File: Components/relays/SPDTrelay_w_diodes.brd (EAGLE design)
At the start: 27.9 x 41.6 mm, 3 parts, among them K1 PY14-02

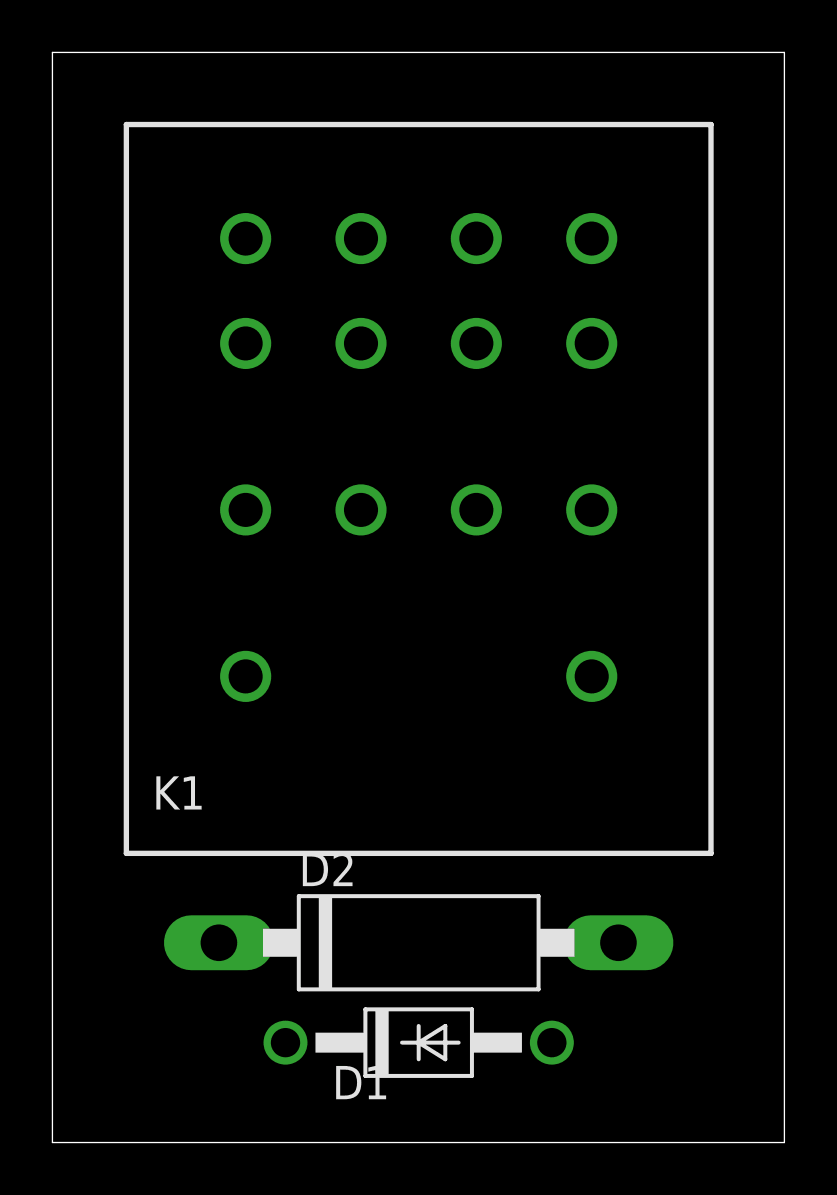
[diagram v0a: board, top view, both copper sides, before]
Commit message: Creating re-usable suppressed relay components w/ vertical diodes
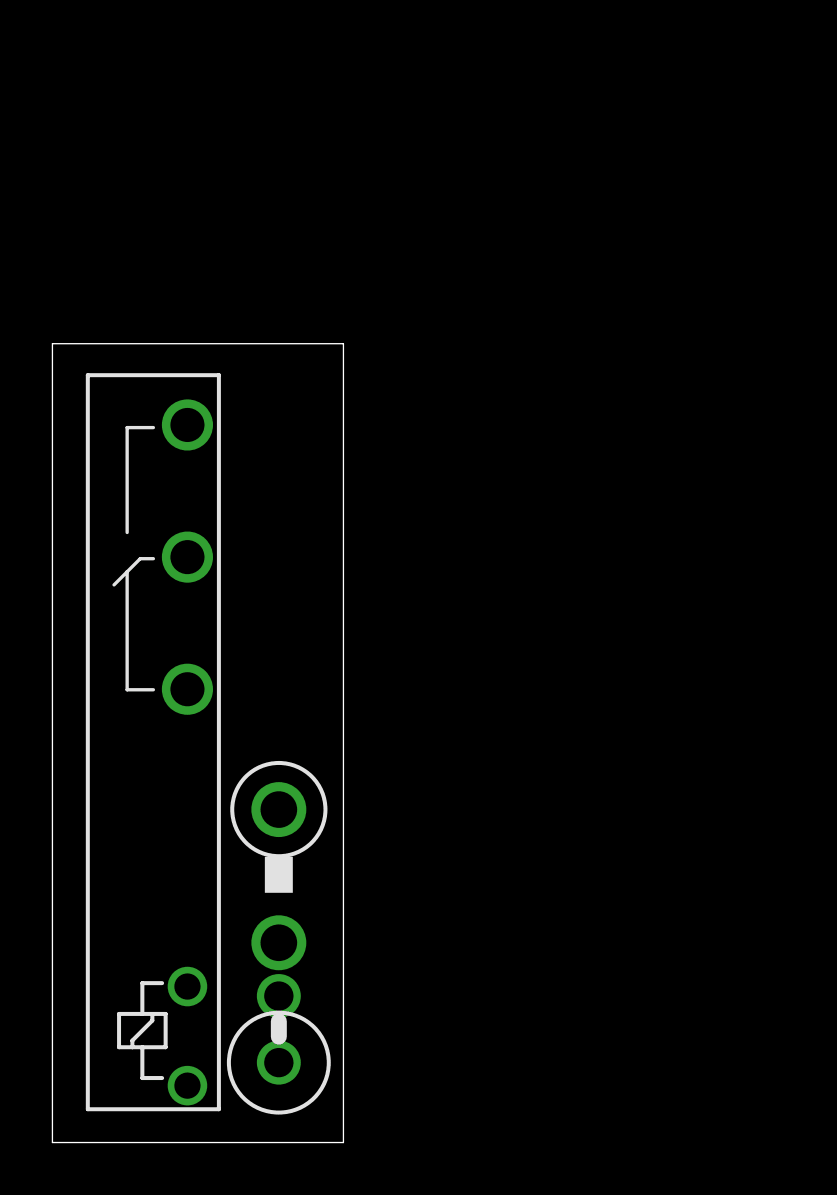
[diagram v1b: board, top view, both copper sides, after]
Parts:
- D1: device relay_computer_custom:DO41-10 -> relay_computer_custom:RAD2,5
- D2: device relay_computer_custom:C1702-15 -> relay_computer_custom:C1702-05
- K1: value PY14-02 -> HF41F-12-Z; device relay_computer_custom:PY14-02 -> relay_computer_custom:HF41F-12-Z
- moved K1 18.2 mm to (6.35, 1.27), turned to 90 degrees
- moved D2 5.91 mm to (8.64, 10.2), turned to 270 degrees
- moved D1 5.36 mm to (8.64, 4.32), turned to 90 degrees
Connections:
- net GND: now also K1.2; no longer K1.A1
- net IN: now also K1.1; no longer K1.A2
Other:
- board size 27.9 x 41.6 mm -> 11.1 x 30.5 mm
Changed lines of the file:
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@@
 <layers>
 <layer number="1" name="Top" color="4" fill="1" visible="yes" active="yes"/>
-<layer number="2" name="Route2" color="1" fill="3" visible="no" active="no"/>
-<layer number="15" name="Route15" color="4" fill="6" visible="no" active="no"/>
 <layer number="16" name="Bottom" color="1" fill="1" visible="yes" active="yes"/>
 <layer number="17" name="Pads" color="2" fill="1" visible="yes" active="yes"/>
@@
 <board>
 <plain>
-<wire x1="0" y1="0" x2="27.92" y2="0" width="0" layer="20"/>
-<wire x1="27.92" y1="0" x2="27.92" y2="41.58" width="0" layer="20"/>
-<wire x1="27.92" y1="41.58" x2="0" y2="41.58" width="0" layer="20"/>
-<wire x1="0" y1="41.58" x2="0" y2="0" width="0" layer="20"/>
+<wire x1="0" y1="0" x2="11.1" y2="0" width="0" layer="20"/>
+<wire x1="11.1" y1="0" x2="11.1" y2="30.47" width="0" layer="20"/>
+<wire x1="11.1" y1="30.47" x2="0" y2="30.47" width="0" layer="20"/>
+<wire x1="0" y1="30.47" x2="0" y2="0" width="0" layer="20"/>
 </plain>
 <attributes>
@@
 </autorouter>
 <elements>
-<element name="D1" library="relay_computer_custom" package="DO41-10" value="1N4007" x="13.97" y="3.81" smashed="yes">
-<attribute name="NAME" x="10.668" y="1.651" size="1.27" layer="25" ratio="10"/>
-<attribute name="VALUE" x="14.478" y="4.826" size="1.27" layer="27" ratio="10"/>
-</element>
-<element name="D2" library="relay_computer_custom" package="C1702-15" value="1N5359" x="13.97" y="7.62" smashed="yes">
-<attribute name="NAME" x="9.398" y="9.779" size="1.27" layer="25" ratio="10"/>
-<attribute name="VALUE" x="13.716" y="10.033" size="1.27" layer="27" ratio="10"/>
-</element>
-<element name="K1" library="relay_computer_custom" package="PY14-02" value="PY14-02" x="13.97" y="17.78">
-<attribute name="MF" value="" x="13.97" y="17.78" size="1.778" layer="27" display="off"/>
-<attribute name="MPN" value="" x="13.97" y="17.78" size="1.778" layer="27" display="off"/>
-<attribute name="OC_FARNELL" value="" x="13.97" y="17.78" size="1.778" layer="27" display="off"/>
-<attribute name="OC_NEWARK" value="" x="13.97" y="17.78" size="1.778" layer="27" display="off"/>
-</element>
+<element name="D1" library="relay_computer_custom" package="RAD2,5" value="1N4007" x="8.636" y="4.318" rot="R90"/>
+<element name="D2" library="relay_computer_custom" package="C1702-05" value="1N5359" x="8.636" y="10.16" rot="R270"/>
+<element name="K1" library="relay_computer_custom" package="HF41F-12-Z" value="HF41F-12-Z" x="6.35" y="1.27" rot="R90"/>
 </elements>
 <signals>
@@
 <contactref element="D1" pad="A"/>
 <contactref element="D2" pad="A"/>
-<wire x1="19.05" y1="3.81" x2="21.59" y2="7.62" width="0" layer="19" extent="1-1"/>
+<wire x1="8.636" y1="5.588" x2="8.636" y2="7.62" width="0" layer="19" extent="1-1"/>
 </signal>
 <signal name="GND">
-<contactref element="K1" pad="A1"/>
 <contactref element="D2" pad="C"/>
-<wire x1="6.35" y1="7.62" x2="20.57" y2="17.78" width="0" layer="19" extent="1-1"/>
+<contactref element="K1" pad="2"/>
+<wire x1="8.636" y1="12.7" x2="5.15" y2="5.95" width="0" layer="19" extent="1-1"/>
 </signal>
 <signal name="IN">
-<contactref element="K1" pad="A2"/>
 <contactref element="D1" pad="C"/>
-<wire x1="8.89" y1="3.81" x2="7.37" y2="17.78" width="0" layer="19" extent="1-1"/>
+<contactref element="K1" pad="1"/>
+<wire x1="8.636" y1="3.048" x2="5.15" y2="2.17" width="0" layer="19" extent="1-1"/>
 </signal>
 </signals>

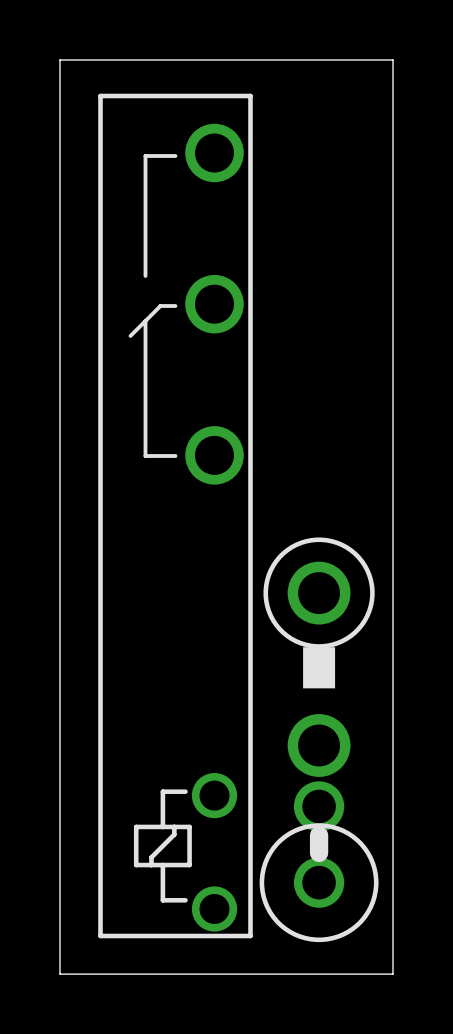
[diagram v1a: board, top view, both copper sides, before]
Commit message: Correcting footprint for SPST and SPDT relays
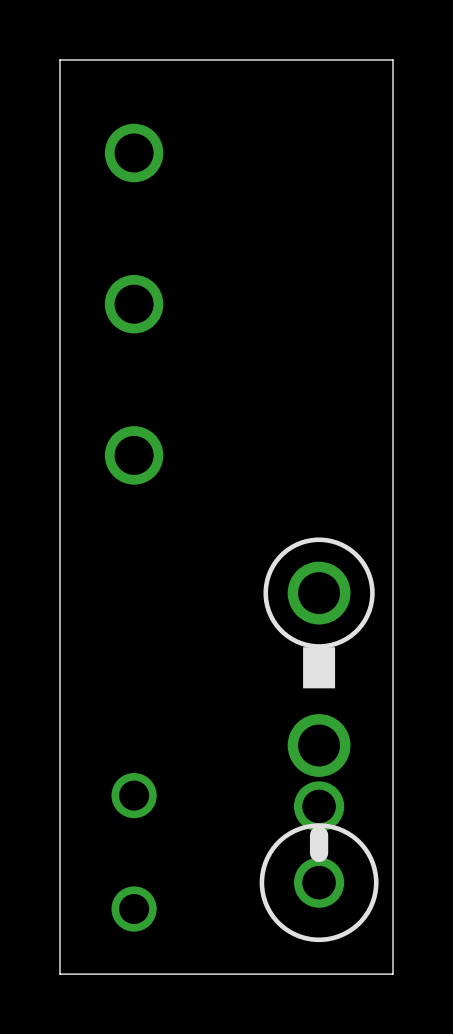
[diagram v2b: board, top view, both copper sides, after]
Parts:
- moved K1 28.4 mm to (1.27, 29.2), turned to 270 degrees
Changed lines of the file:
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@@
 <?xml version="1.0" encoding="utf-8"?>
 <!DOCTYPE eagle SYSTEM "eagle.dtd">
-<eagle version="8.3.2">
+<eagle version="8.7.0">
 <drawing>
 <settings>
@@
 <layers>
 <layer number="1" name="Top" color="4" fill="1" visible="yes" active="yes"/>
+<layer number="2" name="Route2" color="1" fill="3" visible="no" active="no"/>
+<layer number="15" name="Route15" color="4" fill="6" visible="no" active="no"/>
 <layer number="16" name="Bottom" color="1" fill="1" visible="yes" active="yes"/>
 <layer number="17" name="Pads" color="2" fill="1" visible="yes" active="yes"/>
@@
 <param name="dpMaxLengthDifference" value="10mm"/>
 <param name="dpGapFactor" value="2.5"/>
-<param name="checkGrid" value="0"/>
 <param name="checkAngle" value="0"/>
 <param name="checkFont" value="1"/>
 <param name="checkRestrict" value="1"/>
+<param name="checkStop" value="0"/>
+<param name="checkValues" value="0"/>
 <param name="useDiameter" value="13"/>
 <param name="maxErrors" value="50"/>
@@
 <element name="D1" library="relay_computer_custom" package="RAD2,5" value="1N4007" x="8.636" y="4.318" rot="R90"/>
 <element name="D2" library="relay_computer_custom" package="C1702-05" value="1N5359" x="8.636" y="10.16" rot="R270"/>
-<element name="K1" library="relay_computer_custom" package="HF41F-12-Z" value="HF41F-12-Z" x="6.35" y="1.27" rot="R90"/>
+<element name="K1" library="relay_computer_custom" package="HF41F-12-Z" value="HF41F-12-Z" x="1.27" y="29.21" rot="R270"/>
 </elements>
 <signals>
@@
 <contactref element="D2" pad="C"/>
 <contactref element="K1" pad="2"/>
-<wire x1="8.636" y1="12.7" x2="5.15" y2="5.95" width="0" layer="19" extent="1-1"/>
+<wire x1="2.47" y1="5.95" x2="8.636" y2="12.7" width="0" layer="19" extent="1-1"/>
 </signal>
 <signal name="IN">
 <contactref element="D1" pad="C"/>
 <contactref element="K1" pad="1"/>
-<wire x1="8.636" y1="3.048" x2="5.15" y2="2.17" width="0" layer="19" extent="1-1"/>
+<wire x1="8.636" y1="3.048" x2="2.47" y2="2.17" width="0" layer="19" extent="1-1"/>
 </signal>
 </signals>

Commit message: Updating components with latest library updates
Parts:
- D2: value 1N5359 -> 1N5359VERT_SML; device relay_computer_custom:C1702-05 -> relay_computer_custom:RAD2.5_D2
- moved D2 1.27 mm to (8.64, 8.89)
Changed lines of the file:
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@@
 <layer number="48" name="Document" color="7" fill="1" visible="yes" active="yes"/>
 <layer number="49" name="Reference" color="7" fill="1" visible="yes" active="yes"/>
+<layer number="50" name="dxf" color="7" fill="1" visible="no" active="no"/>
 <layer number="51" name="tDocu" color="7" fill="1" visible="yes" active="yes"/>
 <layer number="52" name="bDocu" color="7" fill="1" visible="yes" active="yes"/>
+<layer number="53" name="tGND_GNDA" color="7" fill="9" visible="no" active="no"/>
+<layer number="54" name="bGND_GNDA" color="1" fill="9" visible="no" active="no"/>
+<layer number="56" name="wert" color="7" fill="1" visible="no" active="no"/>
+<layer number="57" name="tCAD" color="7" fill="1" visible="no" active="no"/>
+<layer number="59" name="tCarbon" color="7" fill="1" visible="no" active="no"/>
+<layer number="60" name="bCarbon" color="7" fill="1" visible="no" active="no"/>
 <layer number="90" name="Modules" color="5" fill="1" visible="no" active="no"/>
 <layer number="91" name="Nets" color="2" fill="1" visible="no" active="no"/>
@@
 <layer number="98" name="Guide" color="6" fill="1" visible="no" active="no"/>
 <layer number="99" name="SpiceOrder" color="5" fill="1" visible="no" active="no"/>
+<layer number="100" name="Muster" color="7" fill="1" visible="no" active="no"/>
+<layer number="101" name="Patch_Top" color="12" fill="4" visible="no" active="yes"/>
+<layer number="102" name="Vscore" color="7" fill="1" visible="no" active="yes"/>
+<layer number="103" name="fp3" color="7" fill="1" visible="no" active="yes"/>
+<layer number="104" name="Name" color="7" fill="1" visible="no" active="yes"/>
+<layer number="105" name="Beschreib" color="9" fill="1" visible="no" active="yes"/>
+<layer number="106" name="BGA-Top" color="4" fill="1" visible="no" active="yes"/>
+<layer number="107" name="BD-Top" color="5" fill="1" visible="no" active="yes"/>
+<layer number="108" name="fp8" color="7" fill="1" visible="no" active="yes"/>
+<layer number="109" name="fp9" color="7" fill="1" visible="no" active="yes"/>
+<layer number="110" name="fp0" color="7" fill="1" visible="no" active="yes"/>
+<layer number="111" name="LPC17xx" color="7" fill="1" visible="no" active="yes"/>
+<layer number="112" name="tSilk" color="7" fill="1" visible="no" active="yes"/>
+<layer number="113" name="ReferenceLS" color="7" fill="1" visible="no" active="no"/>
+<layer number="114" name="Badge_Outline" color="7" fill="1" visible="no" active="yes"/>
+<layer number="115" name="ReferenceISLANDS" color="7" fill="1" visible="no" active="yes"/>
+<layer number="116" name="Patch_BOT" color="9" fill="4" visible="no" active="yes"/>
+<layer number="118" name="Rect_Pads" color="7" fill="1" visible="no" active="no"/>
+<layer number="121" name="_tsilk" color="7" fill="1" visible="no" active="yes"/>
+<layer number="122" name="_bsilk" color="7" fill="1" visible="no" active="yes"/>
+<layer number="123" name="tTestmark" color="7" fill="1" visible="no" active="yes"/>
+<layer number="124" name="bTestmark" color="7" fill="1" visible="no" active="yes"/>
+<layer number="125" name="_tNames" color="7" fill="1" visible="no" active="yes"/>
+<layer number="126" name="_bNames" color="7" fill="1" visible="no" active="yes"/>
+<layer number="127" name="_tValues" color="7" fill="1" visible="no" active="yes"/>
+<layer number="128" name="_bValues" color="7" fill="1" visible="no" active="yes"/>
+<layer number="129" name="Mask" color="7" fill="1" visible="no" active="yes"/>
+<layer number="131" name="tAdjust" color="7" fill="1" visible="no" active="yes"/>
+<layer number="132" name="bAdjust" color="7" fill="1" visible="no" active="yes"/>
+<layer number="144" name="Drill_legend" color="7" fill="1" visible="no" active="yes"/>
+<layer number="150" name="Notes" color="7" fill="1" visible="no" active="yes"/>
+<layer number="151" name="HeatSink" color="7" fill="1" visible="no" active="yes"/>
+<layer number="152" name="_bDocu" color="7" fill="1" visible="no" active="yes"/>
+<layer number="153" name="FabDoc1" color="6" fill="1" visible="no" active="no"/>
+<layer number="154" name="FabDoc2" color="2" fill="1" visible="no" active="no"/>
+<layer number="155" name="FabDoc3" color="7" fill="15" visible="no" active="no"/>
+<layer number="199" name="Contour" color="7" fill="1" visible="no" active="yes"/>
+<layer number="200" name="200bmp" color="1" fill="10" visible="no" active="yes"/>
+<layer number="201" name="201bmp" color="2" fill="1" visible="no" active="no"/>
+<layer number="202" name="202bmp" color="3" fill="1" visible="no" active="no"/>
+<layer number="203" name="203bmp" color="4" fill="10" visible="no" active="yes"/>
+<layer number="204" name="204bmp" color="5" fill="10" visible="no" active="yes"/>
+<layer number="205" name="205bmp" color="6" fill="10" visible="no" active="yes"/>
+<layer number="206" name="206bmp" color="7" fill="10" visible="no" active="yes"/>
+<layer number="207" name="207bmp" color="8" fill="10" visible="no" active="yes"/>
+<layer number="208" name="208bmp" color="9" fill="10" visible="no" active="yes"/>
+<layer number="209" name="209bmp" color="7" fill="1" visible="no" active="yes"/>
+<layer number="210" name="210bmp" color="7" fill="1" visible="no" active="yes"/>
+<layer number="211" name="211bmp" color="7" fill="1" visible="no" active="yes"/>
+<layer number="212" name="212bmp" color="7" fill="1" visible="no" active="yes"/>
+<layer number="213" name="213bmp" color="7" fill="1" visible="no" active="yes"/>
+<layer number="214" name="214bmp" color="7" fill="1" visible="no" active="yes"/>
+<layer number="215" name="215bmp" color="7" fill="1" visible="no" active="yes"/>
+<layer number="216" name="216bmp" color="7" fill="1" visible="no" active="yes"/>
+<layer number="217" name="217bmp" color="18" fill="1" visible="no" active="no"/>
+<layer number="218" name="218bmp" color="19" fill="1" visible="no" active="no"/>
+<layer number="219" name="219bmp" color="20" fill="1" visible="no" active="no"/>
+<layer number="220" name="220bmp" color="21" fill="1" visible="no" active="no"/>
+<layer number="221" name="221bmp" color="22" fill="1" visible="no" active="no"/>
+<layer number="222" name="222bmp" color="23" fill="1" visible="no" active="no"/>
+<layer number="223" name="223bmp" color="24" fill="1" visible="no" active="no"/>
+<layer number="224" name="224bmp" color="25" fill="1" visible="no" active="no"/>
+<layer number="225" name="225bmp" color="7" fill="1" visible="no" active="yes"/>
+<layer number="226" name="226bmp" color="7" fill="1" visible="no" active="yes"/>
+<layer number="227" name="227bmp" color="7" fill="1" visible="no" active="yes"/>
+<layer number="228" name="228bmp" color="7" fill="1" visible="no" active="yes"/>
+<layer number="229" name="229bmp" color="7" fill="1" visible="no" active="yes"/>
+<layer number="230" name="230bmp" color="7" fill="1" visible="no" active="yes"/>
+<layer number="231" name="Eagle3D_PG1" color="7" fill="1" visible="no" active="no"/>
+<layer number="232" name="Eagle3D_PG2" color="7" fill="1" visible="no" active="no"/>
+<layer number="233" name="Eagle3D_PG3" color="7" fill="1" visible="no" active="no"/>
+<layer number="248" name="Housing" color="7" fill="1" visible="no" active="yes"/>
+<layer number="249" name="Edge" color="7" fill="1" visible="no" active="yes"/>
+<layer number="250" name="Descript" color="7" fill="1" visible="no" active="no"/>
+<layer number="251" name="SMDround" color="7" fill="1" visible="no" active="no"/>
+<layer number="254" name="cooling" color="7" fill="1" visible="no" active="yes"/>
+<layer number="255" name="routoute" color="7" fill="1" visible="no" active="yes"/>
 </layers>
 <board>
@@
 <elements>
 <element name="D1" library="relay_computer_custom" package="RAD2,5" value="1N4007" x="8.636" y="4.318" rot="R90"/>
-<element name="D2" library="relay_computer_custom" package="C1702-05" value="1N5359" x="8.636" y="10.16" rot="R270"/>
+<element name="D2" library="relay_computer_custom" package="RAD2.5_D2" value="1N5359VERT_SML" x="8.636" y="8.89" rot="R270"/>
 <element name="K1" library="relay_computer_custom" package="HF41F-12-Z" value="HF41F-12-Z" x="1.27" y="29.21" rot="R270"/>
 </elements>
@@
 <contactref element="D2" pad="C"/>
 <contactref element="K1" pad="2"/>
-<wire x1="2.47" y1="5.95" x2="8.636" y2="12.7" width="0" layer="19" extent="1-1"/>
+<wire x1="2.47" y1="5.95" x2="8.636" y2="10.16" width="0" layer="19" extent="1-1"/>
 </signal>
 <signal name="IN">
